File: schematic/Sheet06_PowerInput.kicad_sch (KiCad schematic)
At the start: 9 parts, among them J1 POWER_IN, U10 INA214-SP

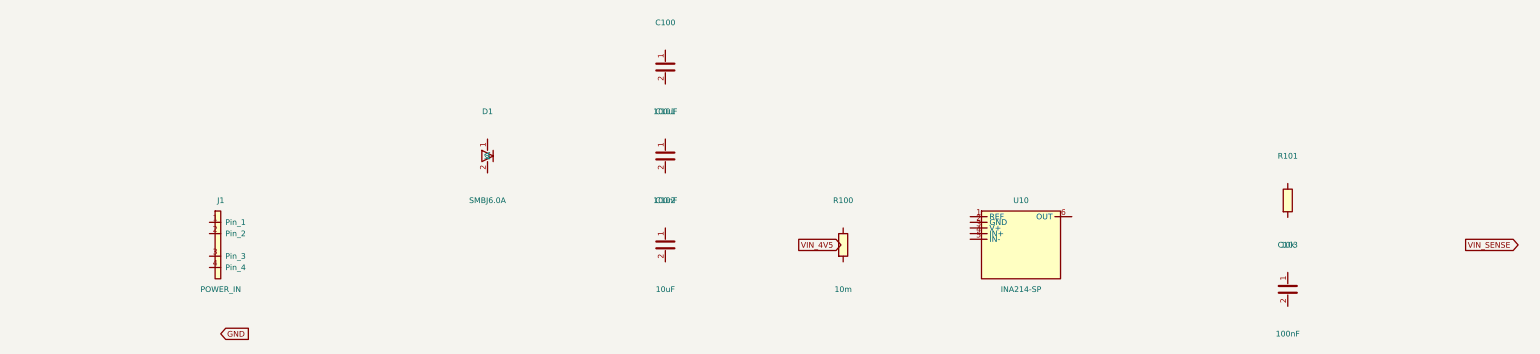
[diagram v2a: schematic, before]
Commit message: feat: add 745 wire connections linking all IC pins to labels and power symbols
- Added stub wires from every component pin to net labels/global_labels
- Power pins connected to correct power symbols (GND, +1V0, +1V8, +3V3, etc.)
- Signal pins connected to labeled nets matching design spec
- Global labels for cross-sheet signals (JESD, SPI, clock, SpaceWire)
- Fixed missing +3V3 power symbol definitions in 5 sheets
- All 17 sheets export successfully with KiCad CLI (17/17 OK)
- Merged PDF: 3.1MB, 17 pages with visible wire connections
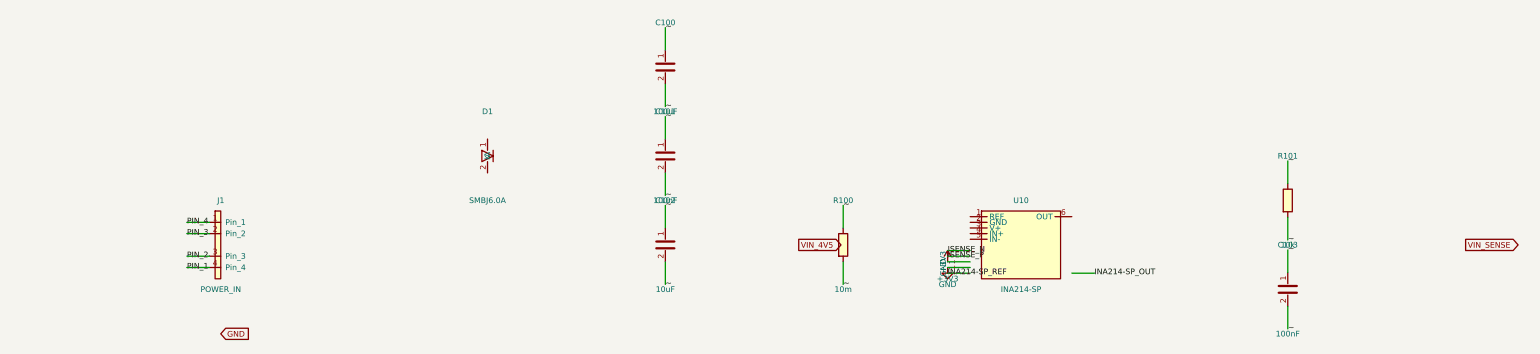
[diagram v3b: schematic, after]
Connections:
- net ~: now reaches C102.1
- net ~: now also C100.1, C100.2, C101.1, C101.2, C102.2, C103.1, C103.2, R100.1, R100.2, R101.1, R101.2
- net PIN_4: now reaches J1.1 (Pin_1)
- net PIN_3: now reaches J1.2 (Pin_2)
- net PIN_2: now reaches J1.3 (Pin_3)
- net PIN_1: now reaches J1.4 (Pin_4)
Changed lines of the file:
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@@
     (pin "1")
     (pin "2")
-  )  (global_label "VIN_4V5" (shape output) (at 190 80 0) (effects (font (size 1.27 1.27)) (justify left)))  (global_label "VIN_SENSE" (shape output) (at 340 80 0) (effects (font (size 1.27 1.27)) (justify left)))  (global_label "GND" (shape input) (at 60 100 0) (effects (font (size 1.27 1.27)) (justify left)))  (sheet_instances (path "/" (page "1")))
+  )  (global_label "VIN_4V5" (shape output) (at 190 80 0) (effects (font (size 1.27 1.27)) (justify left)))  (global_label "VIN_SENSE" (shape output) (at 340 80 0) (effects (font (size 1.27 1.27)) (justify left)))  (global_label "GND" (shape input) (at 60 100 0) (effects (font (size 1.27 1.27)) (justify left)))
+  (wire (pts (xy 57.46 85.08) (xy 52.38 85.08)) (stroke (width 0) (type default)))
+  (label "PIN_1" (at 52.38 85.08 0) (effects (font (size 1.27 1.27))))
+  (wire (pts (xy 57.46 82.54) (xy 52.38 82.54)) (stroke (width 0) (type default)))
+  (label "PIN_2" (at 52.38 82.54 0) (effects (font (size 1.27 1.27))))
+  (wire (pts (xy 57.46 77.46) (xy 52.38 77.46)) (stroke (width 0) (type default)))
+  (label "PIN_3" (at 52.38 77.46 0) (effects (font (size 1.27 1.27))))
+  (wire (pts (xy 57.46 74.92) (xy 52.38 74.92)) (stroke (width 0) (type default)))
+  (label "PIN_4" (at 52.38 74.92 0) (effects (font (size 1.27 1.27))))
+  (wire (pts (xy 160.00 43.81) (xy 160.00 48.89)) (stroke (width 0) (type default)))
+  (label "~" (at 160.00 48.89 0) (effects (font (size 1.27 1.27))))
+  (wire (pts (xy 160.00 36.19) (xy 160.00 31.11)) (stroke (width 0) (type default)))
+  (label "~" (at 160.00 31.11 0) (effects (font (size 1.27 1.27))))
+  (wire (pts (xy 160.00 63.81) (xy 160.00 68.89)) (stroke (width 0) (type default)))
+  (label "~" (at 160.00 68.89 0) (effects (font (size 1.27 1.27))))
+  (wire (pts (xy 160.00 56.19) (xy 160.00 51.11)) (stroke (width 0) (type default)))
+  (label "~" (at 160.00 51.11 0) (effects (font (size 1.27 1.27))))
+  (wire (pts (xy 160.00 83.81) (xy 160.00 88.89)) (stroke (width 0) (type default)))
+  (label "~" (at 160.00 88.89 0) (effects (font (size 1.27 1.27))))
+  (wire (pts (xy 160.00 76.19) (xy 160.00 71.11)) (stroke (width 0) (type default)))
+  (label "~" (at 160.00 71.11 0) (effects (font (size 1.27 1.27))))
+  (wire (pts (xy 228.57 86.35) (xy 223.49 86.35)) (stroke (width 0) (type default)))
+  (label "INA214-SP_REF" (at 223.49 86.35 0) (effects (font (size 1.27 1.27))))
+  (wire (pts (xy 228.57 85.08) (xy 223.49 85.08)) (stroke (width 0) (type default)))
+  (symbol (lib_id "power:GND") (at 223.49 85.08 0) (unit 1)
+      (in_bom yes) (on_board yes) (dnp no)
+      (property "Reference" "#PWRe41" (at 223.49 81.27 0) (effects (font (size 1.27 1.27)) hide))
+      (property "Value" "GND" (at 223.49 88.89 0) (effects (font (size 1.27 1.27))))
+      (property "Footprint" "" (at 0 0 0) (effects (font (size 1.27 1.27)) hide))
+      (property "Datasheet" "" (at 0 0 0) (effects (font (size 1.27 1.27)) hide))
+      (pin "1")
+    )
+  (wire (pts (xy 228.57 83.81) (xy 223.49 83.81)) (stroke (width 0) (type default)))
+  (symbol (lib_id "power:+3V3") (at 223.49 83.81 0) (unit 1)
+      (in_bom yes) (on_board yes) (dnp no)
+      (property "Reference" "#PWR8db" (at 223.49 80.00 0) (effects (font (size 1.27 1.27)) hide))
+      (property "Value" "+3V3" (at 223.49 87.62 0) (effects (font (size 1.27 1.27))))
+      (property "Footprint" "" (at 0 0 0) (effects (font (size 1.27 1.27)) hide))
+      (property "Datasheet" "" (at 0 0 0) (effects (font (size 1.27 1.27)) hide))
+      (pin "1")
+    )
+  (wire (pts (xy 228.57 82.54) (xy 223.49 82.54)) (stroke (width 0) (type default)))
+  (label "ISENSE_P" (at 223.49 82.54 0) (effects (font (size 1.27 1.27))))
+  (wire (pts (xy 228.57 81.27) (xy 223.49 81.27)) (stroke (width 0) (type default)))
+  (label "ISENSE_N" (at 223.49 81.27 0) (effects (font (size 1.27 1.27))))
+  (wire (pts (xy 251.43 86.35) (xy 256.51 86.35)) (stroke (width 0) (type default)))
+  (label "INA214-SP_OUT" (at 256.51 86.35 0) (effects (font (size 1.27 1.27))))
+  (wire (pts (xy 200.00 83.81) (xy 200.00 88.89)) (stroke (width 0) (type default)))
+  (label "~" (at 200.00 88.89 0) (effects (font (size 1.27 1.27))))
+  (wire (pts (xy 200.00 76.19) (xy 200.00 71.11)) (stroke (width 0) (type default)))
+  (label "~" (at 200.00 71.11 0) (effects (font (size 1.27 1.27))))
+  (wire (pts (xy 300.00 73.81) (xy 300.00 78.89)) (stroke (width 0) (type default)))
+  (label "~" (at 300.00 78.89 0) (effects (font (size 1.27 1.27))))
+  (wire (pts (xy 300.00 66.19) (xy 300.00 61.11)) (stroke (width 0) (type default)))
+  (label "~" (at 300.00 61.11 0) (effects (font (size 1.27 1.27))))
+  (wire (pts (xy 300.00 93.81) (xy 300.00 98.89)) (stroke (width 0) (type default)))
+  (label "~" (at 300.00 98.89 0) (effects (font (size 1.27 1.27))))
+  (wire (pts (xy 300.00 86.19) (xy 300.00 81.11)) (stroke (width 0) (type default)))
+  (label "~" (at 300.00 81.11 0) (effects (font (size 1.27 1.27))))
+  (sheet_instances (path "/" (page "1")))
 )

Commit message: Fix KiCad schematic wiring: Y-inversion bug + all 891 pins connected
- Fixed critical Y-axis inversion bug: KiCad inverts Y when placing
  symbols (lib Y + schematic Y = abs Y is WRONG; correct: abs Y = sym Y - lib Y)
- This caused ALL wires to connect to wrong pins (e.g., CS label connected
  to BG pin instead of CS pin)
- Verified with netlist: 0 unconnected nets, all pin functions correct
- Fixed wire direction for angle 90/270 (swapped due to Y-inversion)
- 891 pin connections across 15 sheets, all 17 sheets export without errors
- Netlist verification: CS→E8, BG→C3, INA+→A4, CLK+→F1, JESD pairs correct

Co-Authored-By: opencode <noreply@opencode.ai>
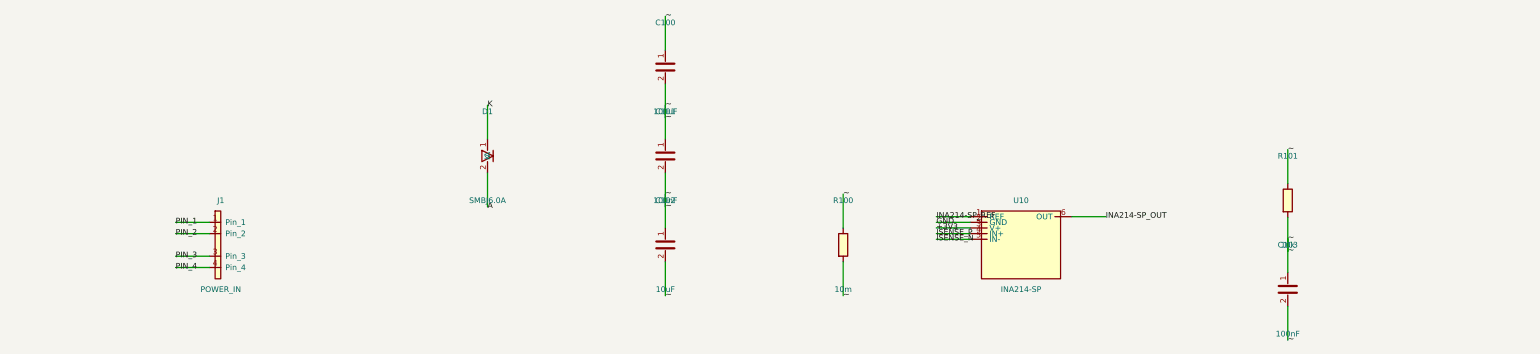
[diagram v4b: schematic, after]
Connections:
- net +3V3: now also U10.3 (V+)
- net GND: now also U10.2 (GND)
- net INA214-SP_OUT: now also U10.6 (OUT)
- net INA214-SP_REF: now also U10.1 (REF)
- net ISENSE_N: now also U10.5 (IN-)
- net ISENSE_P: now also U10.4 (IN+)
- net PIN_1: now also J1.1 (Pin_1); no longer J1.4 (Pin_4)
- net PIN_2: now also J1.2 (Pin_2); no longer J1.3 (Pin_3)
- net PIN_3: now also J1.3 (Pin_3); no longer J1.2 (Pin_2)
- net PIN_4: now also J1.4 (Pin_4); no longer J1.1 (Pin_1)
- net K: now reaches D1.1 (K)
- net A: now reaches D1.2 (A)
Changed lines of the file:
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@@
     (pin "1")
     (pin "2")
-  )  (global_label "VIN_4V5" (shape output) (at 190 80 0) (effects (font (size 1.27 1.27)) (justify left)))  (global_label "VIN_SENSE" (shape output) (at 340 80 0) (effects (font (size 1.27 1.27)) (justify left)))  (global_label "GND" (shape input) (at 60 100 0) (effects (font (size 1.27 1.27)) (justify left)))
-  (wire (pts (xy 57.46 85.08) (xy 52.38 85.08)) (stroke (width 0) (type default)))
-  (label "PIN_1" (at 52.38 85.08 0) (effects (font (size 1.27 1.27))))
-  (wire (pts (xy 57.46 82.54) (xy 52.38 82.54)) (stroke (width 0) (type default)))
-  (label "PIN_2" (at 52.38 82.54 0) (effects (font (size 1.27 1.27))))
-  (wire (pts (xy 57.46 77.46) (xy 52.38 77.46)) (stroke (width 0) (type default)))
-  (label "PIN_3" (at 52.38 77.46 0) (effects (font (size 1.27 1.27))))
-  (wire (pts (xy 57.46 74.92) (xy 52.38 74.92)) (stroke (width 0) (type default)))
-  (label "PIN_4" (at 52.38 74.92 0) (effects (font (size 1.27 1.27))))
-  (wire (pts (xy 160.00 43.81) (xy 160.00 48.89)) (stroke (width 0) (type default)))
-  (label "~" (at 160.00 48.89 0) (effects (font (size 1.27 1.27))))
-  (wire (pts (xy 160.00 36.19) (xy 160.00 31.11)) (stroke (width 0) (type default)))
-  (label "~" (at 160.00 31.11 0) (effects (font (size 1.27 1.27))))
-  (wire (pts (xy 160.00 63.81) (xy 160.00 68.89)) (stroke (width 0) (type default)))
-  (label "~" (at 160.00 68.89 0) (effects (font (size 1.27 1.27))))
-  (wire (pts (xy 160.00 56.19) (xy 160.00 51.11)) (stroke (width 0) (type default)))
-  (label "~" (at 160.00 51.11 0) (effects (font (size 1.27 1.27))))
-  (wire (pts (xy 160.00 83.81) (xy 160.00 88.89)) (stroke (width 0) (type default)))
-  (label "~" (at 160.00 88.89 0) (effects (font (size 1.27 1.27))))
-  (wire (pts (xy 160.00 76.19) (xy 160.00 71.11)) (stroke (width 0) (type default)))
-  (label "~" (at 160.00 71.11 0) (effects (font (size 1.27 1.27))))
-  (wire (pts (xy 228.57 86.35) (xy 223.49 86.35)) (stroke (width 0) (type default)))
-  (label "INA214-SP_REF" (at 223.49 86.35 0) (effects (font (size 1.27 1.27))))
-  (wire (pts (xy 228.57 85.08) (xy 223.49 85.08)) (stroke (width 0) (type default)))
-  (symbol (lib_id "power:GND") (at 223.49 85.08 0) (unit 1)
-      (in_bom yes) (on_board yes) (dnp no)
-      (property "Reference" "#PWRe41" (at 223.49 81.27 0) (effects (font (size 1.27 1.27)) hide))
-      (property "Value" "GND" (at 223.49 88.89 0) (effects (font (size 1.27 1.27))))
-      (property "Footprint" "" (at 0 0 0) (effects (font (size 1.27 1.27)) hide))
-      (property "Datasheet" "" (at 0 0 0) (effects (font (size 1.27 1.27)) hide))
-      (pin "1")
-    )
-  (wire (pts (xy 228.57 83.81) (xy 223.49 83.81)) (stroke (width 0) (type default)))
-  (symbol (lib_id "power:+3V3") (at 223.49 83.81 0) (unit 1)
-      (in_bom yes) (on_board yes) (dnp no)
-      (property "Reference" "#PWR8db" (at 223.49 80.00 0) (effects (font (size 1.27 1.27)) hide))
-      (property "Value" "+3V3" (at 223.49 87.62 0) (effects (font (size 1.27 1.27))))
-      (property "Footprint" "" (at 0 0 0) (effects (font (size 1.27 1.27)) hide))
-      (property "Datasheet" "" (at 0 0 0) (effects (font (size 1.27 1.27)) hide))
-      (pin "1")
-    )
-  (wire (pts (xy 228.57 82.54) (xy 223.49 82.54)) (stroke (width 0) (type default)))
-  (label "ISENSE_P" (at 223.49 82.54 0) (effects (font (size 1.27 1.27))))
-  (wire (pts (xy 228.57 81.27) (xy 223.49 81.27)) (stroke (width 0) (type default)))
-  (label "ISENSE_N" (at 223.49 81.27 0) (effects (font (size 1.27 1.27))))
-  (wire (pts (xy 251.43 86.35) (xy 256.51 86.35)) (stroke (width 0) (type default)))
-  (label "INA214-SP_OUT" (at 256.51 86.35 0) (effects (font (size 1.27 1.27))))
-  (wire (pts (xy 200.00 83.81) (xy 200.00 88.89)) (stroke (width 0) (type default)))
-  (label "~" (at 200.00 88.89 0) (effects (font (size 1.27 1.27))))
-  (wire (pts (xy 200.00 76.19) (xy 200.00 71.11)) (stroke (width 0) (type default)))
-  (label "~" (at 200.00 71.11 0) (effects (font (size 1.27 1.27))))
-  (wire (pts (xy 300.00 73.81) (xy 300.00 78.89)) (stroke (width 0) (type default)))
-  (label "~" (at 300.00 78.89 0) (effects (font (size 1.27 1.27))))
-  (wire (pts (xy 300.00 66.19) (xy 300.00 61.11)) (stroke (width 0) (type default)))
-  (label "~" (at 300.00 61.11 0) (effects (font (size 1.27 1.27))))
-  (wire (pts (xy 300.00 93.81) (xy 300.00 98.89)) (stroke (width 0) (type default)))
-  (label "~" (at 300.00 98.89 0) (effects (font (size 1.27 1.27))))
-  (wire (pts (xy 300.00 86.19) (xy 300.00 81.11)) (stroke (width 0) (type default)))
-  (label "~" (at 300.00 81.11 0) (effects (font (size 1.27 1.27))))
+  )
+  (wire (pts (xy 57.4600 74.9200) (xy 49.8400 74.9200)) (stroke (width 0) (type default)))
+  (label "PIN_1" (at 49.8400 74.9200 0) (effects (font (size 1.27 1.27))))
+  (wire (pts (xy 57.4600 77.4600) (xy 49.8400 77.4600)) (stroke (width 0) (type default)))
+  (label "PIN_2" (at 49.8400 77.4600 0) (effects (font (size 1.27 1.27))))
+  (wire (pts (xy 57.4600 82.5400) (xy 49.8400 82.5400)) (stroke (width 0) (type default)))
+  (label "PIN_3" (at 49.8400 82.5400 0) (effects (font (size 1.27 1.27))))
+  (wire (pts (xy 57.4600 85.0800) (xy 49.8400 85.0800)) (stroke (width 0) (type default)))
+  (label "PIN_4" (at 49.8400 85.0800 0) (effects (font (size 1.27 1.27))))
+  (wire (pts (xy 120.0000 56.1900) (xy 120.0000 48.5700)) (stroke (width 0) (type default)))
+  (label "K" (at 120.0000 48.5700 0) (effects (font (size 1.27 1.27))))
+  (wire (pts (xy 120.0000 63.8100) (xy 120.0000 71.4300)) (stroke (width 0) (type default)))
+  (label "A" (at 120.0000 71.4300 0) (effects (font (size 1.27 1.27))))
+  (wire (pts (xy 160.0000 36.1900) (xy 160.0000 28.5700)) (stroke (width 0) (type default)))
+  (label "~" (at 160.0000 28.5700 0) (effects (font (size 1.27 1.27))))
+  (wire (pts (xy 160.0000 43.8100) (xy 160.0000 51.4300)) (stroke (width 0) (type default)))
+  (label "~" (at 160.0000 51.4300 0) (effects (font (size 1.27 1.27))))
+  (wire (pts (xy 160.0000 56.1900) (xy 160.0000 48.5700)) (stroke (width 0) (type default)))
+  (label "~" (at 160.0000 48.5700 0) (effects (font (size 1.27 1.27))))
+  (wire (pts (xy 160.0000 63.8100) (xy 160.0000 71.4300)) (stroke (width 0) (type default)))
+  (label "~" (at 160.0000 71.4300 0) (effects (font (size 1.27 1.27))))
+  (wire (pts (xy 160.0000 76.1900) (xy 160.0000 68.5700)) (stroke (width 0) (type default)))
+  (label "~" (at 160.0000 68.5700 0) (effects (font (size 1.27 1.27))))
+  (wire (pts (xy 160.0000 83.8100) (xy 160.0000 91.4300)) (stroke (width 0) (type default)))
+  (label "~" (at 160.0000 91.4300 0) (effects (font (size 1.27 1.27))))
+  (wire (pts (xy 228.5700 73.6500) (xy 220.9500 73.6500)) (stroke (width 0) (type default)))
+  (label "INA214-SP_REF" (at 220.9500 73.6500 0) (effects (font (size 1.27 1.27))))
+  (wire (pts (xy 228.5700 74.9200) (xy 220.9500 74.9200)) (stroke (width 0) (type default)))
+  (label "GND" (at 220.9500 74.9200 0) (effects (font (size 1.27 1.27))))
+  (wire (pts (xy 228.5700 76.1900) (xy 220.9500 76.1900)) (stroke (width 0) (type default)))
+  (label "+3V3" (at 220.9500 76.1900 0) (effects (font (size 1.27 1.27))))
+  (wire (pts (xy 228.5700 77.4600) (xy 220.9500 77.4600)) (stroke (width 0) (type default)))
+  (label "ISENSE_P" (at 220.9500 77.4600 0) (effects (font (size 1.27 1.27))))
+  (wire (pts (xy 228.5700 78.7300) (xy 220.9500 78.7300)) (stroke (width 0) (type default)))
+  (label "ISENSE_N" (at 220.9500 78.7300 0) (effects (font (size 1.27 1.27))))
+  (wire (pts (xy 251.4300 73.6500) (xy 259.0500 73.6500)) (stroke (width 0) (type default)))
+  (label "INA214-SP_OUT" (at 259.0500 73.6500 0) (effects (font (size 1.27 1.27))))
+  (wire (pts (xy 200.0000 76.1900) (xy 200.0000 68.5700)) (stroke (width 0) (type default)))
+  (label "~" (at 200.0000 68.5700 0) (effects (font (size 1.27 1.27))))
+  (wire (pts (xy 200.0000 83.8100) (xy 200.0000 91.4300)) (stroke (width 0) (type default)))
+  (label "~" (at 200.0000 91.4300 0) (effects (font (size 1.27 1.27))))
+  (wire (pts (xy 300.0000 66.1900) (xy 300.0000 58.5700)) (stroke (width 0) (type default)))
+  (label "~" (at 300.0000 58.5700 0) (effects (font (size 1.27 1.27))))
+  (wire (pts (xy 300.0000 73.8100) (xy 300.0000 81.4300)) (stroke (width 0) (type default)))
+  (label "~" (at 300.0000 81.4300 0) (effects (font (size 1.27 1.27))))
+  (wire (pts (xy 300.0000 86.1900) (xy 300.0000 78.5700)) (stroke (width 0) (type default)))
+  (label "~" (at 300.0000 78.5700 0) (effects (font (size 1.27 1.27))))
+  (wire (pts (xy 300.0000 93.8100) (xy 300.0000 101.4300)) (stroke (width 0) (type default)))
+  (label "~" (at 300.0000 101.4300 0) (effects (font (size 1.27 1.27))))
   (sheet_instances (path "/" (page "1")))
 )
